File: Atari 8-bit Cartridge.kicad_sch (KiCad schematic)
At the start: 8 parts, among them J1 Atari 8-bit Left Cartridge Co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, U0 27C128, U1 27C64

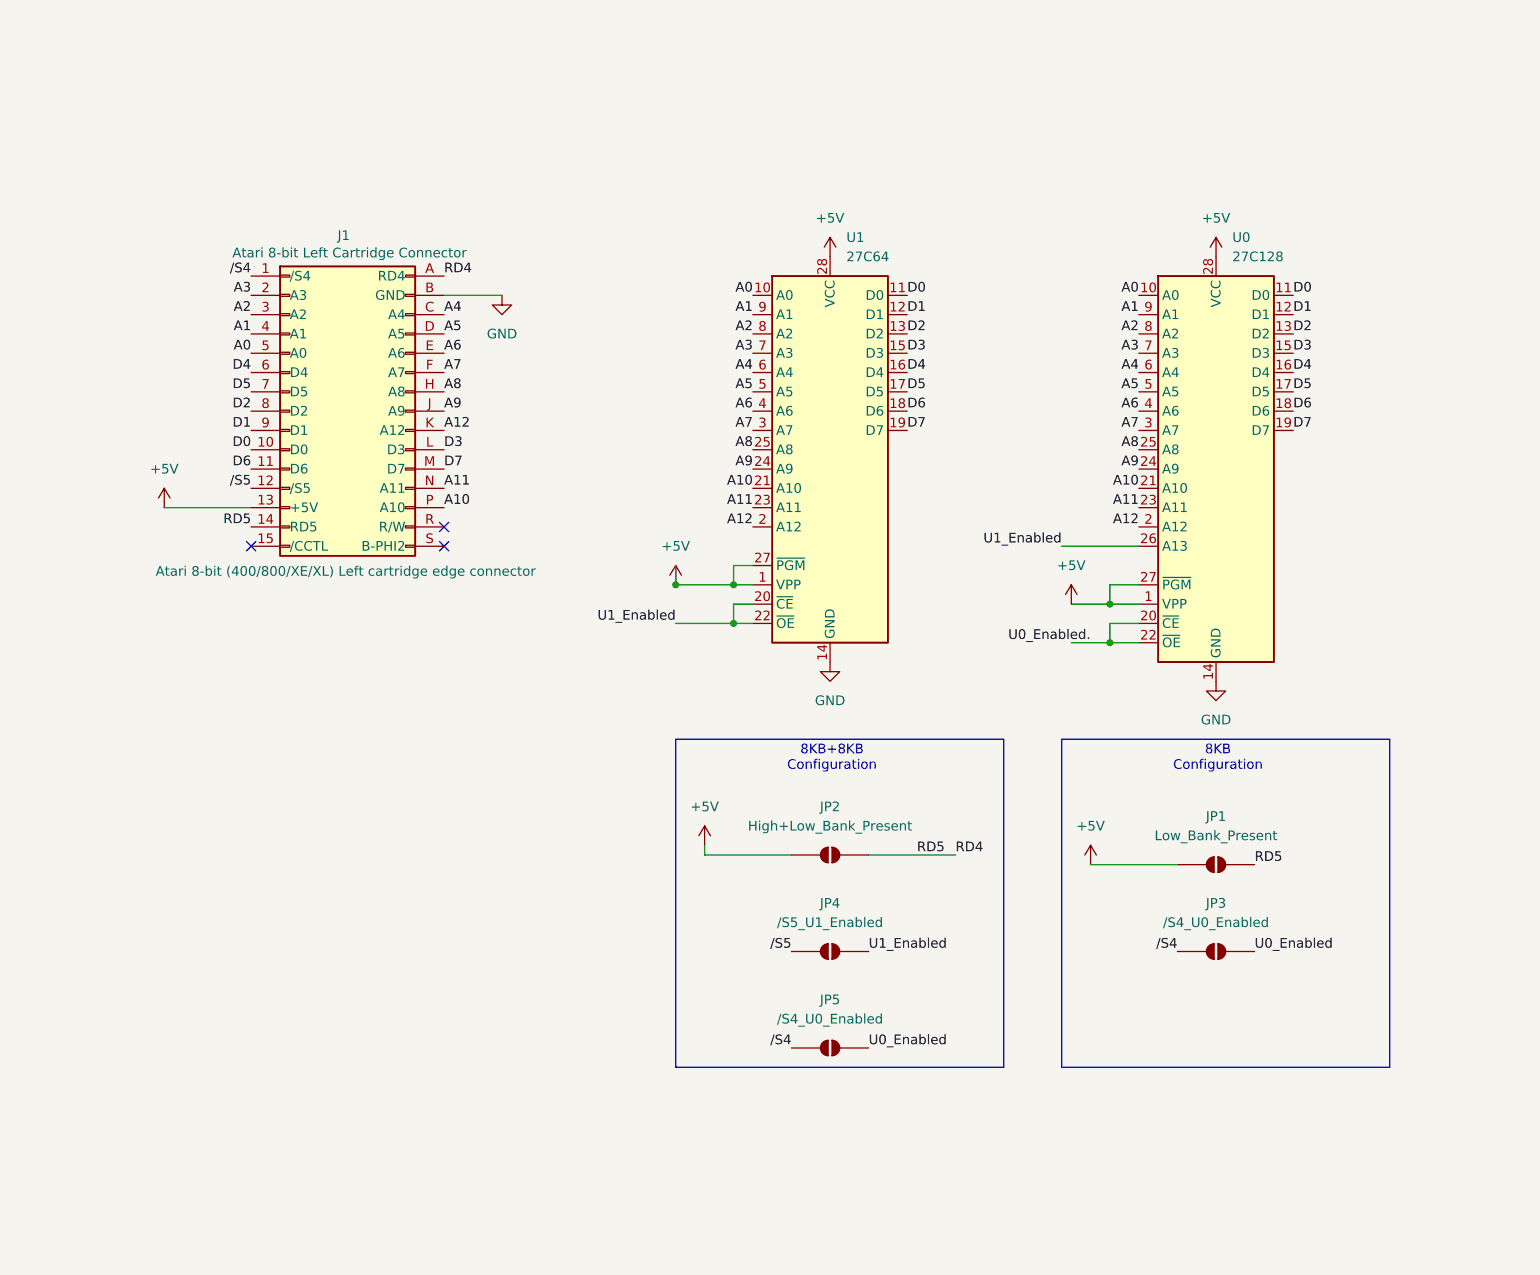
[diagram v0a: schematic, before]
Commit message: Create footprint for cart edge connector.
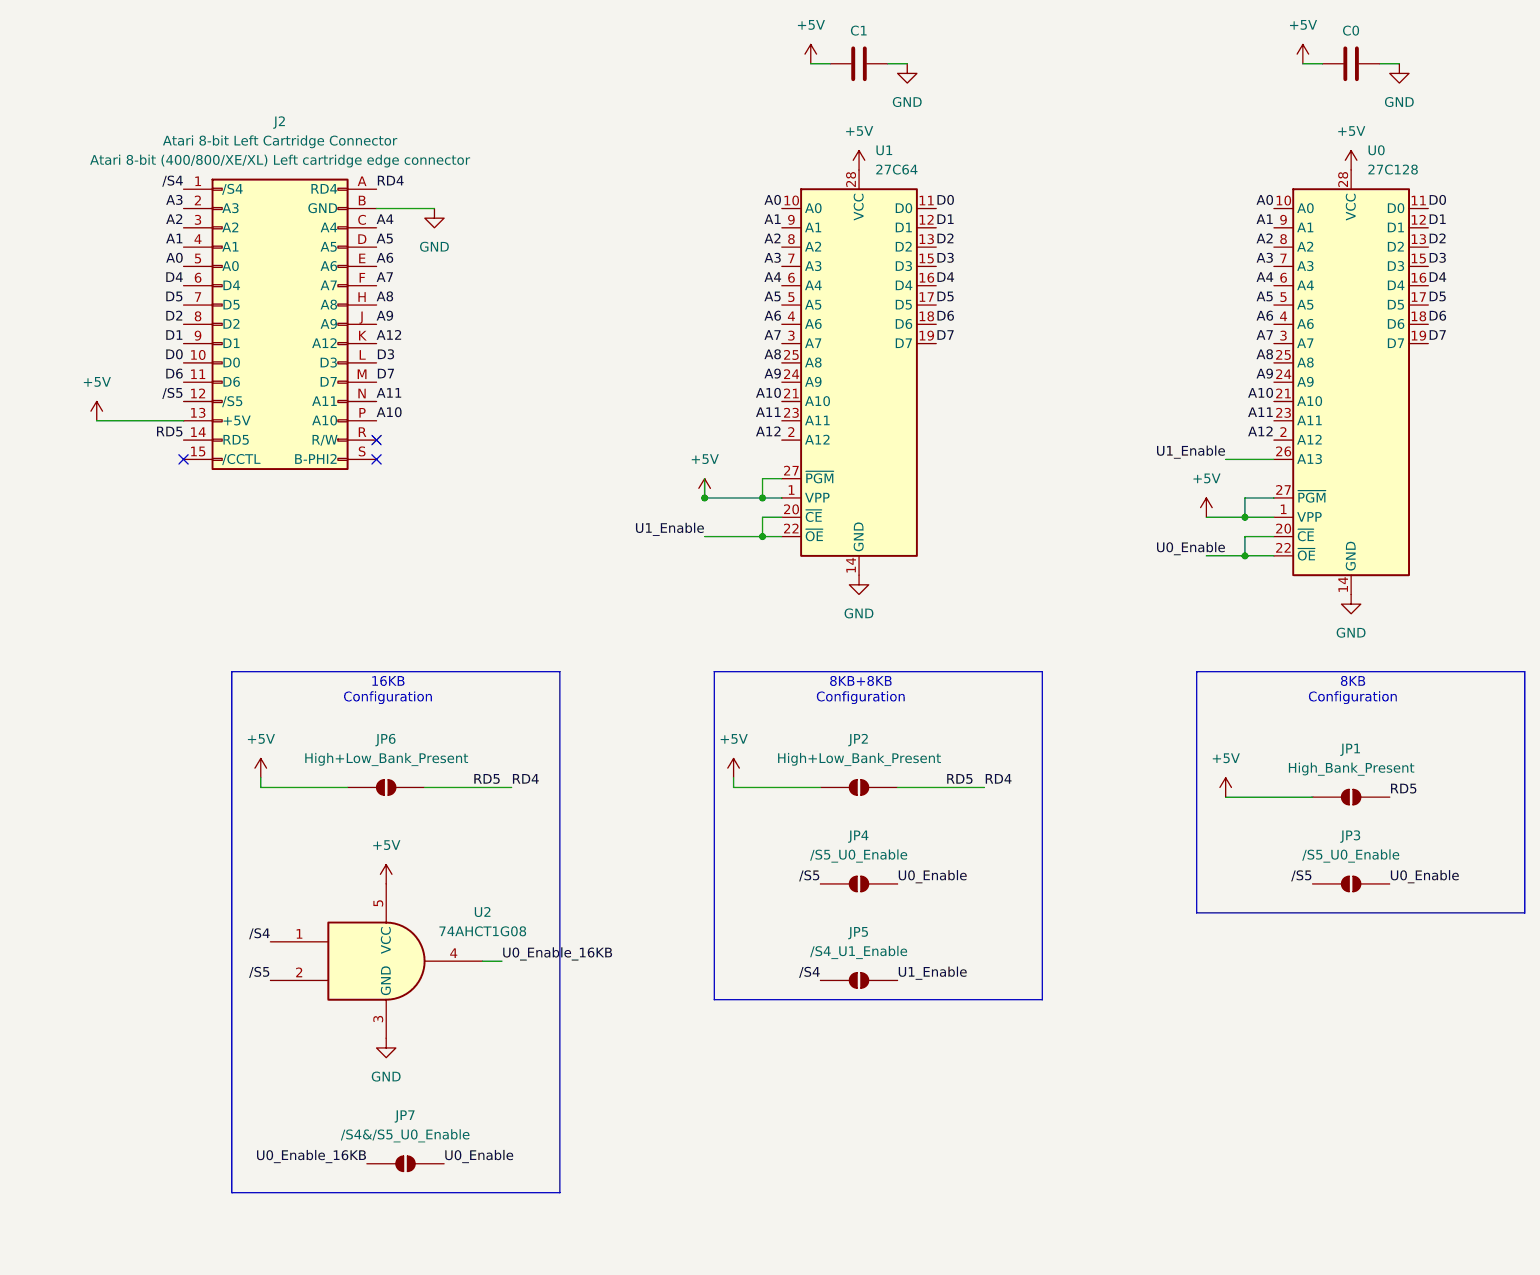
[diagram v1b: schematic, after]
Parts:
- removed J1: Atari 8-bit Left Cartridge Connector, symbol Connector_Generic:Conn_02x15_Row_Letter_First
- added C0, C1: C, Capacitor_THT:C_Disc_D7.5mm_W5.0mm_P5.00mm, symbol Device:C
- added J2: Atari 8-bit Left Cartridge Connector, Atari_8-bit:Atari_8-bit_Cartridge_Connector, symbol Atari_8-bit:Atari_8-bit_Left_Cartridge_Connector
- added JP6: High+Low_Bank_Present, Jumper:SolderJumper-2_P1.3mm_Open_RoundedPad1.0x1.5mm, symbol Jumper:SolderJumper_2_Open
- added JP7: /S4&/S5_U0_Enable, Jumper:SolderJumper-2_P1.3mm_Open_RoundedPad1.0x1.5mm, symbol Jumper:SolderJumper_2_Open
- added U2: 74AHCT1G08, Package_TO_SOT_SMD:SOT-353_SC-70-5, symbol 74xGxx:74AHCT1G08
- JP1: value Low_Bank_Present -> High_Bank_Present; footprint (none) -> Jumper:SolderJumper-2_P1.3mm_Open_RoundedPad1.0x1.5mm
- JP2: footprint (none) -> Jumper:SolderJumper-2_P1.3mm_Open_RoundedPad1.0x1.5mm
- JP3: value /S4_U0_Enabled -> /S5_U0_Enable; footprint (none) -> Jumper:SolderJumper-2_P1.3mm_Open_RoundedPad1.0x1.5mm
- JP4: value /S5_U1_Enabled -> /S5_U0_Enable; footprint (none) -> Jumper:SolderJumper-2_P1.3mm_Open_RoundedPad1.0x1.5mm
- JP5: value /S4_U0_Enabled -> /S4_U1_Enable; footprint (none) -> Jumper:SolderJumper-2_P1.3mm_Open_RoundedPad1.0x1.5mm
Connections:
- net U0_Enabled. is gone; now on net U0_Enable: U0.20 (~{CE}), U0.22 (~{OE})
- net +5V: now also C0.1, C1.1, J2.13 (+5V), JP6.1 (A), U2.5 (VCC)
- net A0: now also J2.5 (A0)
- net A1: now also J2.4 (A1)
- net A10: now also J2.P (A10)
- net A11: now also J2.N (A11)
- net A12: now also J2.K (A12)
- net A2: now also J2.3 (A2)
- net A3: now also J2.2 (A3)
- net A4: now also J2.C (A4)
- net A5: now also J2.D (A5)
- net A6: now also J2.E (A6)
- net A7: now also J2.F (A7)
- net A8: now also J2.H (A8)
- net A9: now also J2.J (A9)
- net D0: now also J2.10 (D0)
- net D1: now also J2.9 (D1)
- net D2: now also J2.8 (D2)
- net D3: now also J2.L (D3)
- net D4: now also J2.6 (D4)
- net D5: now also J2.7 (D5)
- net D6: now also J2.11 (D6)
- net D7: now also J2.M (D7)
- net GND: now also C0.2, C1.2, J2.B (GND), U2.3 (GND)
- net RD4: now also J2.14 (RD5), J2.A (RD4), JP6.2 (B)
- net /S4: now also J2.1 (/S4), U2.1; no longer JP3.1 (A)
- net /S5: now also JP3.1 (A), J2.12 (/S5), U2.2
- net U0_Enabled renamed U0_Enable
- net U0_Enable: now also JP4.2 (B), JP7.1 (A); no longer JP5.2 (B)
- net U1_Enabled renamed U1_Enable
- net U1_Enable: now also JP5.2 (B); no longer JP4.2 (B)
- new net U0_Enable_16KB: JP7.2 (B), U2.4
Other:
- note added: "16KB Configuration"
- moved on the sheet: JP1, JP2, JP3, JP4, JP5, U0, U1

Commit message: Lay out configuration jumpers.
This required moving quite a bit around to make room.
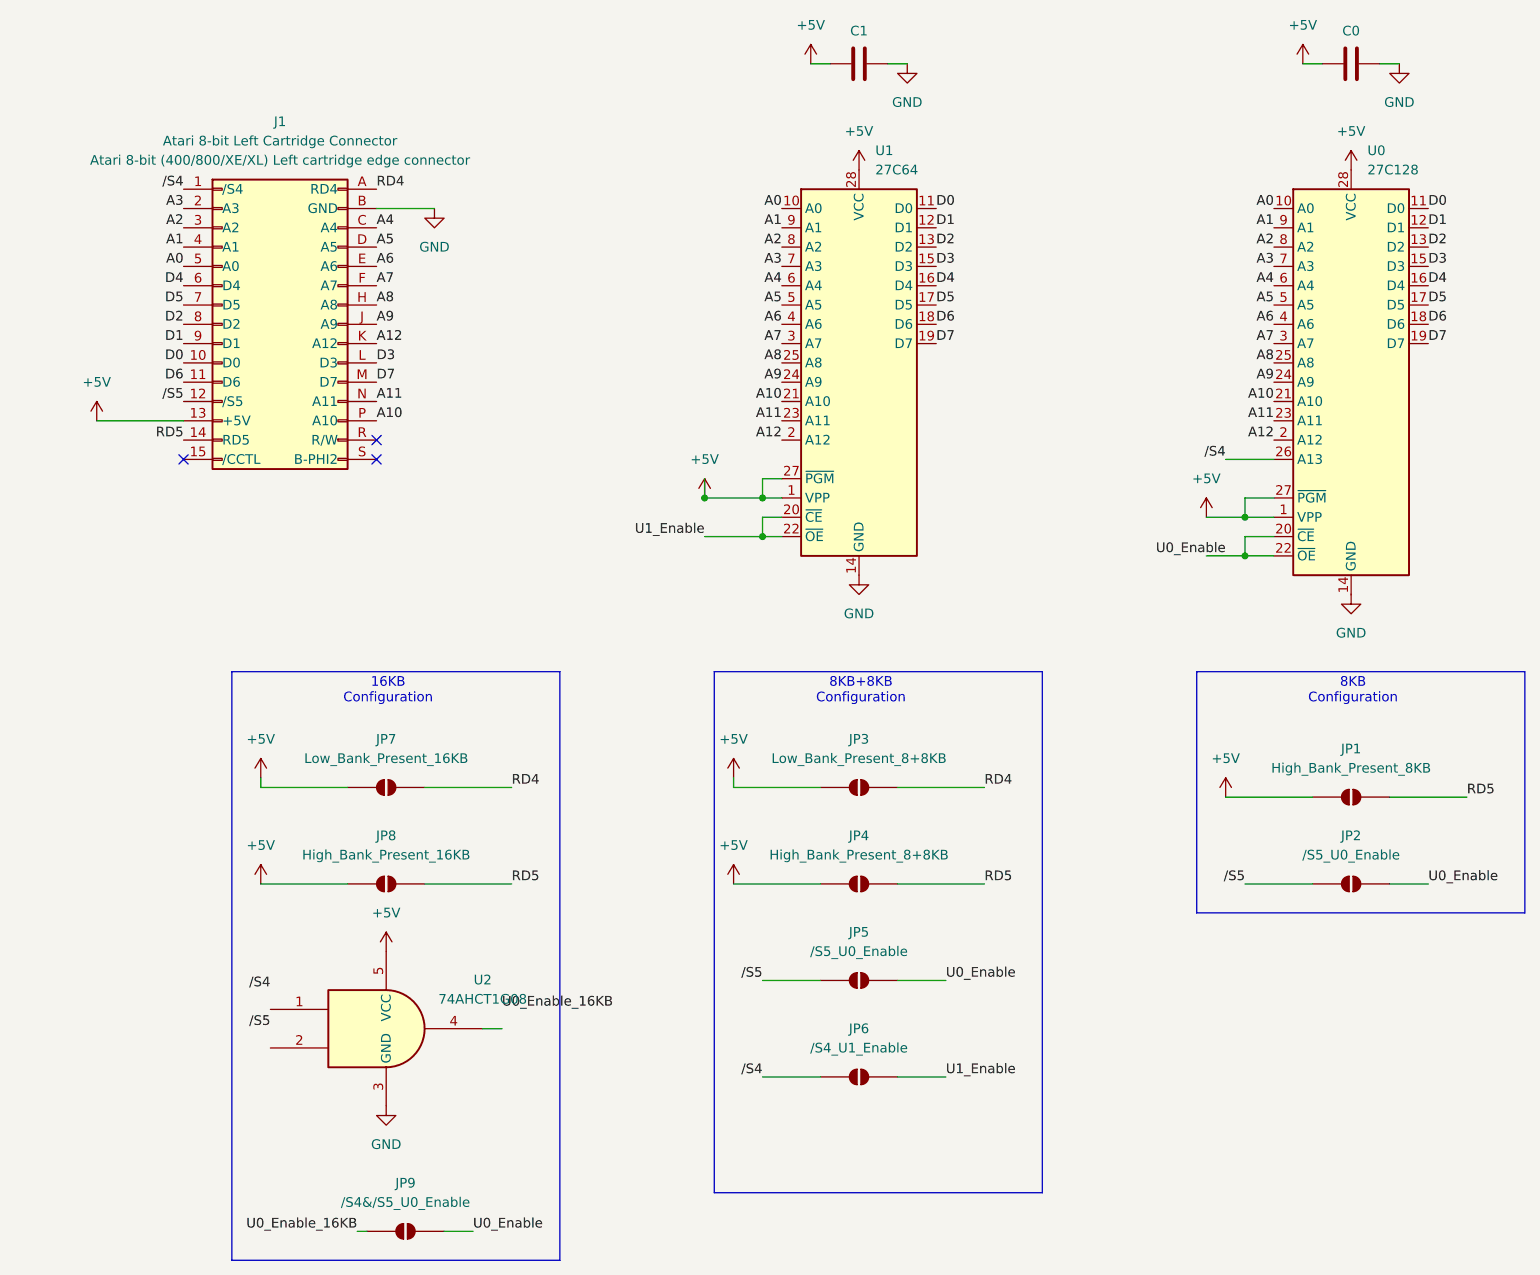
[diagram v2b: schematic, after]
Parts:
- removed JP6: High+Low_Bank_Present, Jumper:SolderJumper-2_P1.3mm_Open_RoundedPad1.0x1.5mm, symbol Jumper:SolderJumper_2_Open
- added JP4: High_Bank_Present_8+8KB, Atari_8-bit:SolderJumper, symbol Jumper:SolderJumper_2_Open
- added JP7: Low_Bank_Present_16KB, Atari_8-bit:SolderJumper, symbol Jumper:SolderJumper_2_Open
- added JP8: High_Bank_Present_16KB, Atari_8-bit:SolderJumper, symbol Jumper:SolderJumper_2_Open
- C0, C1: value C -> 100nF; footprint Capacitor_THT:C_Disc_D7.5mm_W5.0mm_P5.00mm -> Capacitor_THT:C_Disc_D5.0mm_W2.5mm_P5.00mm
- JP1: value High_Bank_Present -> High_Bank_Present_8KB; footprint Jumper:SolderJumper-2_P1.3mm_Open_RoundedPad1.0x1.5mm -> Atari_8-bit:SolderJumper
- JP2: renamed from JP3; footprint Jumper:SolderJumper-2_P1.3mm_Open_RoundedPad1.0x1.5mm -> Atari_8-bit:SolderJumper
- JP3: renamed from JP2; value High+Low_Bank_Present -> Low_Bank_Present_8+8KB; footprint Jumper:SolderJumper-2_P1.3mm_Open_RoundedPad1.0x1.5mm -> Atari_8-bit:SolderJumper
- JP5: renamed from JP4; footprint Jumper:SolderJumper-2_P1.3mm_Open_RoundedPad1.0x1.5mm -> Atari_8-bit:SolderJumper
- JP6: renamed from JP5; footprint Jumper:SolderJumper-2_P1.3mm_Open_RoundedPad1.0x1.5mm -> Atari_8-bit:SolderJumper
- JP9: renamed from JP7; footprint Jumper:SolderJumper-2_P1.3mm_Open_RoundedPad1.0x1.5mm -> Atari_8-bit:SolderJumper
- renumbered J2 to J1
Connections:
- net +5V: now also JP4.1 (A), JP7.1 (A), JP8.1 (A)
- net RD4: now also JP7.2 (B); no longer J1.14 (RD5), JP1.2 (B)
- net U0_Enable_16KB: no longer U2.4
- net U1_Enable: no longer U0.26 (A13)
- net /S4: now also U0.26 (A13); no longer U2.1
- net /S5: no longer U2.2
- new net RD5: J1.14 (RD5), JP1.2 (B), JP4.2 (B), JP8.2 (B)
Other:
- moved on the sheet: JP5, JP6, JP9, U2

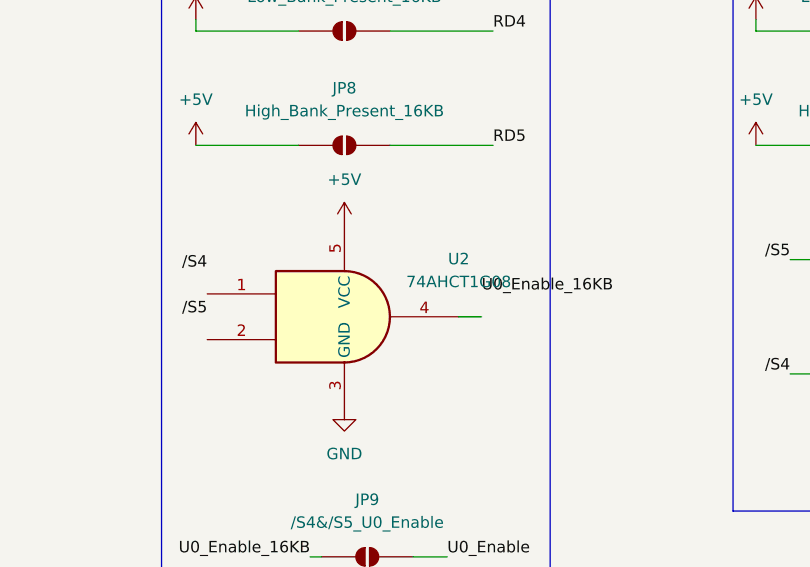
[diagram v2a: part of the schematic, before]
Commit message: First routing pass of back copper.
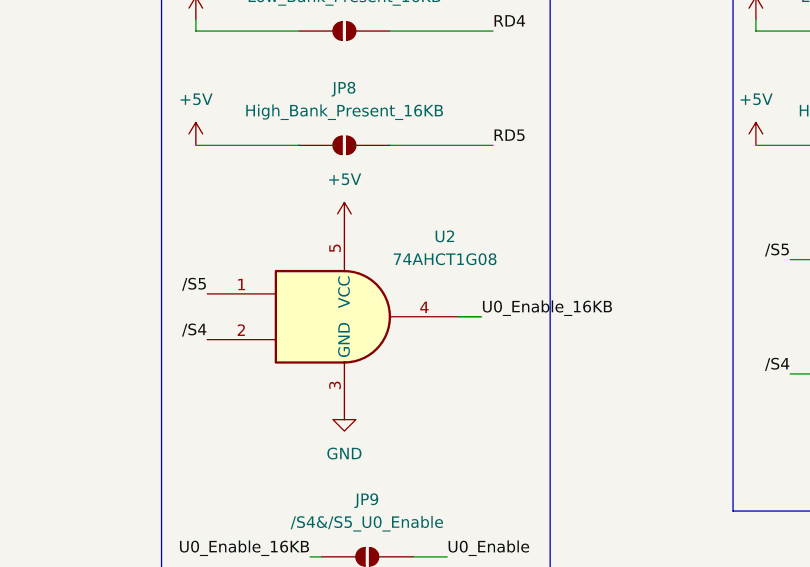
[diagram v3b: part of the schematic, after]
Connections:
- net U0_Enable_16KB: now also U2.4
- net /S4: now also U2.2
- net /S5: now also U2.1
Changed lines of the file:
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@@
 	)
 	(label "U0_Enable_16KB"
-		(at 78.74 147.32 0)
+		(at 78.74 149.86 0)
 		(effects
 			(font
@@
 	)
 	(label "{slash}S4"
-		(at 48.26 144.78 180)
+		(at 48.26 152.4 180)
 		(effects
 			(font
@@
 	)
 	(label "{slash}S5"
-		(at 48.26 149.86 180)
+		(at 48.26 147.32 180)
 		(effects
 			(font
@@
 		(in_pos_files yes)
 		(dnp no)
-		(fields_autoplaced yes)
 		(property "Reference" "U2"
-			(at 76.2 143.4398 0)
+			(at 74.676 140.97 0)
 			(show_name no)
 			(do_not_autoplace no)
@@
 		)
 		(property "Value" "74AHCT1G08"
-			(at 76.2 145.9798 0)
-			(show_name no)
-			(do_not_autoplace no)
+			(at 74.676 143.51 0)
+			(show_name no)
+			(do_not_autoplace no)
